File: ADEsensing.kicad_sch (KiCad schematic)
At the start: 2 parts, among them U5 ADE7953xCP, Y1 Crystal

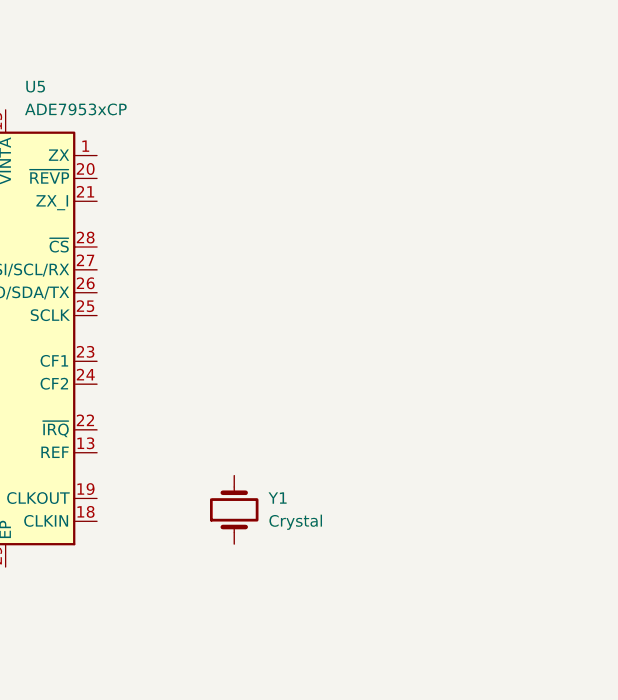
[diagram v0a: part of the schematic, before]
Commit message: added ADE periph
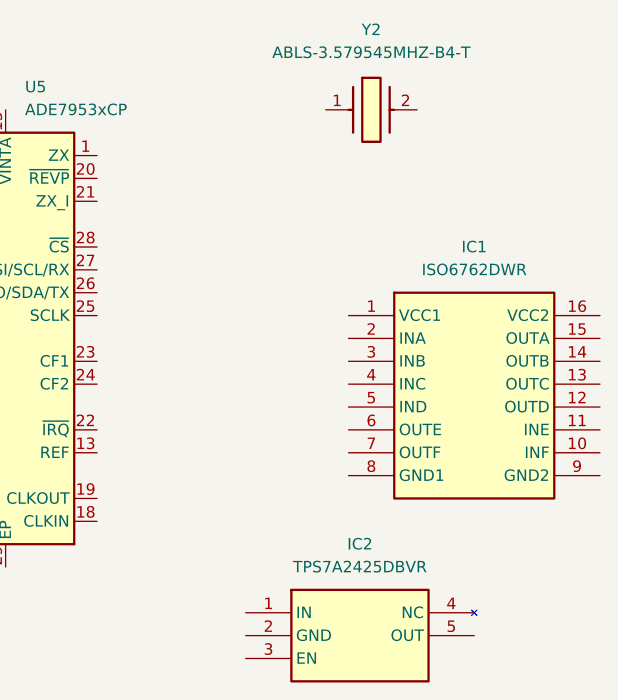
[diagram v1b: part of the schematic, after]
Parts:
- removed Y1: Crystal, symbol Device:Crystal
- added IC1: ISO6762DWR, SOIC127P1030X265-16N, symbol SamacSys_Parts:ISO6762DWR
- added IC2: TPS7A2425DBVR, SOT95P280X145-5N, symbol SamacSys_Parts:TPS7A2425DBVR
- added Y2: ABLS-3.579545MHZ-B4-T, ABLS3579545MHZB4T, symbol SamacSys_Parts:ABLS-3.579545MHZ-B4-T
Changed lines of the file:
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@@
 	(generator_version "10.0")
 	(paper "A4")
-	(symbol
-		(lib_id "Sensor:ADE7953xCP")
-		(at 91.44 87.63 0)
-		(unit 1)
-		(body_style 1)
-		(exclude_from_sim no)
-		(in_bom yes)
-		(on_board yes)
-		(in_pos_files yes)
-		(dnp no)
-		(fields_autoplaced yes)
-		(property "Reference" "U5"
-			(at 96.1233 59.69 0)
-			(show_name no)
-			(do_not_autoplace no)
-			(effects
-				(font
-					(size 1.27 1.27)
-				)
-				(justify left)
-			)
-		)
-		(property "Value" "ADE7953xCP"
-			(at 96.1233 62.23 0)
-			(show_name no)
-			(do_not_autoplace no)
-			(effects
-				(font
-					(size 1.27 1.27)
-				)
-				(justify left)
-			)
-		)
-		(property "Footprint" "Package_CSP:LFCSP-28-1EP_5x5mm_P0.5mm_EP3.14x3.14mm"
-			(at 97.79 116.84 0)
-			(hide yes)
-			(show_name no)
-			(do_not_autoplace no)
-			(effects
-				(font
-					(size 1.27 1.27)
-				)
-				(justify left)
-			)
-		)
-		(property "Datasheet" "https://www.analog.com/media/en/technical-documentation/data-sheets/ADE7953.pdf"
-			(at 99.06 59.69 0)
-			(hide yes)
-			(show_name no)
-			(do_not_autoplace no)
-			(effects
-				(font
-					(size 1.27 1.27)
-				)
-			)
-		)
-		(property "Description" "Single Phase Multifunction Energy Metering with Neutral Current Measurement, LFCSP-28"
-			(at 91.44 87.63 0)
-			(hide yes)
-			(show_name no)
-			(do_not_autoplace no)
-			(effects
-				(font
-					(size 1.27 1.27)
-				)
-			)
-		)
-		(pin "5"
-		)
-		(pin "4"
-		)
-		(pin "7"
-		)
-		(pin "13"
-		)
-		(pin "11"
-		)
-		(pin "1"
-		)
-		(pin "2"
-		)
-		(pin "9"
-		)
-		(pin "6"
-		)
-		(pin "3"
-		)
-		(pin "8"
-		)
-		(pin "12"
-		)
-		(pin "10"
-		)
-		(pin "17"
-		)
-		(pin "22"
-		)
-		(pin "14"
-		)
-		(pin "21"
-		)
-		(pin "27"
-		)
-		(pin "15"
-		)
-		(pin "24"
-		)
-		(pin "28"
-		)
-		(pin "20"
-		)
-		(pin "16"
-		)
-		(pin "29"
-		)
-		(pin "18"
-		)
-		(pin "23"
-		)
-		(pin "26"
-		)
-		(pin "19"
-		)
-		(pin "25"
-		)
-		(instances
-			(project "smart_supply"
-				(path "/487ef637-7a03-4925-80c1-798e0c6f0bbd/21684dc7-d3bf-41d6-9154-934c515daf55"
-					(reference "U5")
-					(unit 1)
-				)
-			)
-		)
-	)
-	(symbol
-		(lib_id "Device:Crystal")
-		(at 119.38 106.68 90)
-		(unit 1)
-		(body_style 1)
-		(exclude_from_sim no)
-		(in_bom yes)
-		(on_board yes)
-		(in_pos_files yes)
-		(dnp no)
-		(fields_autoplaced yes)
-		(property "Reference" "Y1"
-			(at 123.19 105.4099 90)
-			(show_name no)
-			(do_not_autoplace no)
-			(effects
-				(font
-					(size 1.27 1.27)
-				)
-				(justify right)
-			)
-		)
-		(property "Value" "Crystal"
-			(at 123.19 107.9499 90)
-			(show_name no)
-			(do_not_autoplace no)
-			(effects
-				(font
-					(size 1.27 1.27)
-				)
-				(justify right)
-			)
-		)
-		(property "Footprint" ""
-			(at 119.38 106.68 0)
-			(hide yes)
-			(show_name no)
-			(do_not_autoplace no)
-			(effects
-				(font
-					(size 1.27 1.27)
-				)
-			)
-		)
-		(property "Datasheet" ""
-			(at 119.38 106.68 0)
-			(hide yes)
-			(show_name no)
-			(do_not_autoplace no)
-			(effects
-				(font
-					(size 1.27 1.27)
-				)
-			)
-		)
-		(property "Description" "Two pin crystal"
-			(at 119.38 106.68 0)
-			(hide yes)
-			(show_name no)
-			(do_not_autoplace no)
-			(effects
-				(font
-					(size 1.27 1.27)
-				)
-			)
-		)
-		(pin "1"
-		)
-		(pin "2"
-		)
-		(instances
-			(project "smart_supply"
-				(path "/487ef637-7a03-4925-80c1-798e0c6f0bbd/21684dc7-d3bf-41d6-9154-934c515daf55"
-					(reference "Y1")
-					(unit 1)
-				)
-			)
-		)
-	)
-)

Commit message: ade7953 breakout board
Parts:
- removed Y2: ABLS-3.579545MHZ-B4-T, ABLS3579545MHZB4T, symbol SamacSys_Parts:ABLS-3.579545MHZ-B4-T
- added C15, C18: 20p, Capacitor_SMD:C_0603_1608Metric, symbol Device:C
- added C19, C21, C24, C26: 100n, Capacitor_SMD:C_0603_1608Metric, symbol Device:C
- added C20, C22, C23, C25: 4.7u, Capacitor_SMD:C_0805_2012Metric, symbol Device:C
- added C27: 10u, Capacitor_SMD:C_0805_2012Metric, symbol Device:C
- added D5: LED, LED_SMD:LED_0805_2012Metric, symbol Device:LED
- added FB2: FerriteBead_Small, Inductor_SMD:L_0805_2012Metric, symbol Device:FerriteBead_Small
- added J2: Conn_01x05_Pin, Connector_PinHeader_2.54mm:PinHeader_1x05_P2.54mm_Vertical, symbol Connector:Conn_01x05_Pin
- added J3: Conn_01x02_Pin, Connector_PinHeader_2.54mm:PinHeader_1x02_P2.54mm_Vertical, symbol Connector:Conn_01x02_Pin
- added J4, J5: Conn_01x06_Pin, Connector_PinHeader_2.54mm:PinHeader_1x06_P2.54mm_Vertical, symbol Connector:Conn_01x06_Pin
- added R11: 10k, Resistor_SMD:R_0805_2012Metric, symbol Device:R
- added R12: 50, Resistor_SMD:R_0805_2012Metric, symbol Device:R
- added U7: MCP1825ST-3302E/EB, SmartSupplyLib:DDPAK3_MC_MCH, symbol SmartSupplyLib:MCP1825ST-3302E_EB
- added Y1: 3.58M, Crystal:Crystal_SMD_HC49-SD, symbol Device:Crystal
- IC1, IC2: now not fitted; now left out of the parts list
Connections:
- net ZX: now reaches U5.1 (ZX)
- net ZX: now also J5.1 (Pin_1)
- net IBN: now reaches U5.10 (IBN)
- net IBN: now also J4.4 (Pin_4)
- net VN: now reaches U5.11 (VN)
- net VN: now also J4.5 (Pin_5)
- net VP: now reaches U5.12 (VP)
- net VP: now also J4.6 (Pin_6)
- net REF: now reaches U5.13 (REF)
- net REF: now also C25.2, C26.2
- net GND: now reaches U5.14 (PULL_LOW)
- net GND: now also U5.16 (AGND), U5.29 (EP), U5.4 (DGND), C15.1, C18.2, C19.1, C20.1, C22.1, C23.1, C24.1, C25.1, C26.1, C27.2, D5.1 (K), J3.2 (Pin_2), U7.2 (GND), U7.4 (GND)
- net VINTA: now reaches U5.15 (VINTA)
- net VINTA: now also C19.2, C20.2
- net +3.3V: now reaches U5.17 (VDD)
- net +3.3V: now also U5.7 (PULL_HIGH), U5.8 (PULL_HIGH), C27.1, R11.1, R12.1, U7.3 (VOUT)
- net CLKIN: now reaches U5.18 (CLKIN)
- net CLKIN: now also C18.1, Y1.1
- net CLKOUT: now reaches U5.19 (CLKOUT)
- net CLKOUT: now also C15.2, Y1.2
- net RESET: now reaches U5.2 (~{RESET})
- net RESET: now also C21.1, R11.2
- net REVP: now reaches U5.20 (~{REVP})
- net REVP: now also J5.6 (Pin_6)
- net ZX_I: now reaches U5.21 (ZX_I)
- net ZX_I: now also J5.5 (Pin_5)
- net IRQ: now reaches U5.22 (~{IRQ})
- net IRQ: now also J5.4 (Pin_4)
- net CF1: now reaches U5.23 (CF1)
- net CF1: now also J5.3 (Pin_3)
- net CF2: now reaches U5.24 (CF2)
- net CF2: now also J5.2 (Pin_2)
- net SCLK: now reaches U5.25 (SCLK)
- net SCLK: now also J2.4 (Pin_4)
- net MISO: now reaches U5.26 (MISO/SDA/TX)
- net MISO: now also J2.3 (Pin_3)
- net MOSI: now reaches U5.27 (MOSI/SCL/RX)
- net MOSI: now also J2.2 (Pin_2)
- net CS: now reaches U5.28 (~{CS})
- net CS: now also J2.1 (Pin_1)
- net VINTD: now reaches U5.3 (VINTD)
- net VINTD: now also C23.2, C24.2
- net IAP: now reaches U5.5 (IAP)
- net IAP: now also J4.1 (Pin_1)
- net IAN: now reaches U5.6 (IAN)
- net IAN: now also J4.2 (Pin_2)
- net IBP: now reaches U5.9 (IBP)
- net IBP: now also J4.3 (Pin_3)
- new net: D5.2 (A), R12.2
- new net: FB2.1, J3.1 (Pin_1)
- new net +5V: C22.2, FB2.2, U7.1 (VIN)
- new net EN: C21.2, J2.5 (Pin_5)
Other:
- note added: "ADC Input"
- note added: "Comms"
- note added: "Configurable Output"
- note added: "Decoupling"
- note added: "IC"
- note added: "LED_{OK}"
- note added: "Linear voltage regulator"
- note added: "Oscillator"
- note added: "Power"
- note added: "Pull-ups"
- moved on the sheet: U5

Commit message: add mounting holes, 3d models and small fixes
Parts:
- added H1, H2, H3, H4: MountingHole, MountingHole:MountingHole_2.7mm_M2.5, symbol Mechanical:MountingHole
- U5: footprint Package_CSP:LFCSP-28-1EP_5x5mm_P0.5mm_EP3.14x3.14mm -> SmartSupplyLib:LFCSP-28-1EP_5x5mm_P0.5mm_EP3.14x3.14mm_ThermalVias

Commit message: add MPN
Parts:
- C15, C18: MPN (none) -> C165732
- C19, C21, C24, C26: MPN (none) -> C1590
- C20, C22, C23, C25: MPN (none) -> C1779
- C27: MPN (none) -> C15850
- D5: MPN (none) -> C2986046
- FB2: MPN (none) -> C1015
- R11: MPN (none) -> C17414
- R12: MPN (none) -> C55205334
- U5: MPN (none) -> C515890
- U7: footprint SmartSupplyLib:DDPAK3_MC_MCH -> DDPAK3_MC_MCH; MPN (none) -> C632677
- Y1: MPN (none) -> C22464956

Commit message: footprint
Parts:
- U7: footprint DDPAK3_MC_MCH -> SmartSupplyLib:DDPAK3_MC_MCH

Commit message: change ldo to a smaller one
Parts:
- removed U7: MCP1825ST-3302E/EB, SmartSupplyLib:DDPAK3_MC_MCH, symbol SmartSupplyLib:MCP1825ST-3302E_EB
- added U7: MCP1825ST-3302E/DB, Package_TO_SOT_SMD:SOT-223-3_TabPin2, symbol SmartSupplyLib:MCP1825ST-3302E_DB
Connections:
- net +3.3V: now also U7.3 (VOUT)
- net +5V: now also U7.1 (VIN)
- net GND: now also U7.2 (GND)
